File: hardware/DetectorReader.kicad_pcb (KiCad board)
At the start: 2 copper layers, 51.8 x 30 mm, 62 parts, among them J1 10118194-0001LF, J2 Combo_Conn, J3 SMA_Conn, J4 SMA_Conn, J5 SMA_Conn, J6 Conn_Signal, J7 Conn_Amp1, J8 Conn_Amp2, J9 Conn_TriggerOut, Q1 BC847C,215, Q2 BC847C,215, SW1 SeqTrig_SW, U1 ATtiny814-SS, U2 FT231XS-R, U3 XC0900P-10S, U4 MIC5317-3.0YD5-TR, U5 MAX41462GUB+, U6 BA4584RF-E2, U7 MAX4003, Y1 ECS-160-12-37B-CTN-TR

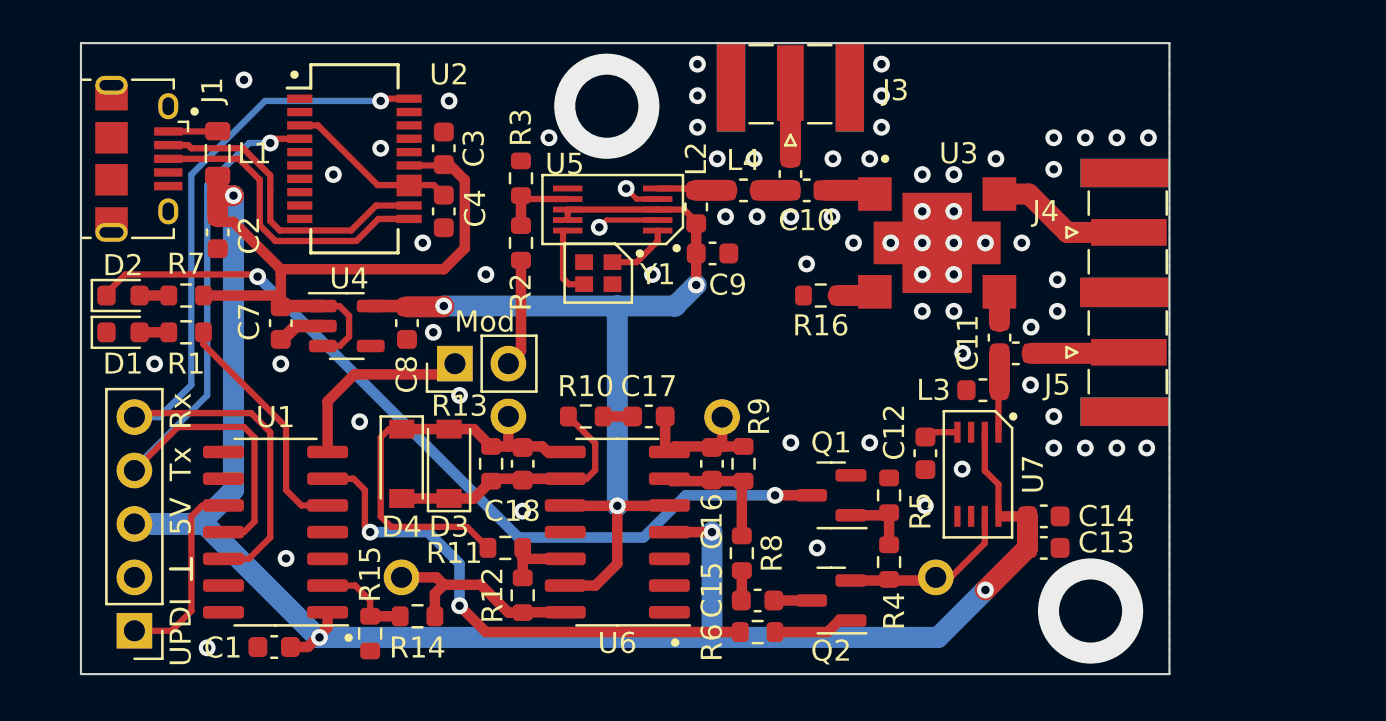
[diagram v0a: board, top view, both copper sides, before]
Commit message: splitted quad opamp into dual opamp and comparator for better digitalization and smaller board
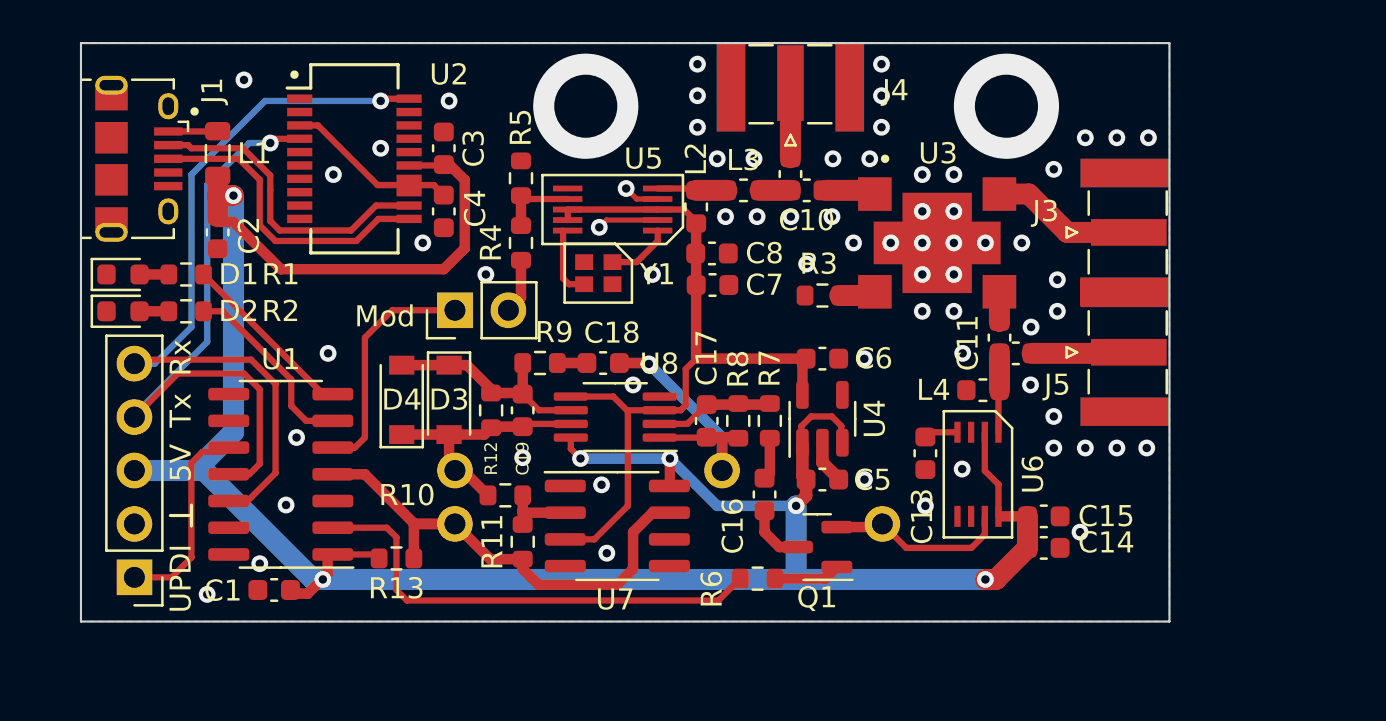
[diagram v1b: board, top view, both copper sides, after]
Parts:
- removed the D2 at (112.0, 84.0)
- removed the Q1 at (145.7, 93.5)
- removed R14: 4.7k, Resistor_SMD:R_0603_1608Metric
- removed R15: 10k, Resistor_SMD:R_0603_1608Metric
- removed the R4 at (148.4, 96.7)
- removed the R5 at (148.4, 93.5)
- removed the R7 at (115.0, 84.0)
- removed the U6 at (135.5, 95.2)
- added C8: 100p, Capacitor_SMD:C_0603_1608Metric, F.Cu at (140.0, 82.0)
- added D1: 150060GS75000, LED_SMD:LED_0603_1608Metric, F.Cu at (112.0, 83.0)
- added R1: 1k, Resistor_SMD:R_0603_1608Metric, F.Cu at (115.0, 83.0)
- added R13: 1k, Resistor_SMD:R_0603_1608Metric, F.Cu at (125.0, 96.5)
- added U7: BA4580RFVM-TR, Package_SO:MSOP-8_3x3mm_P0.65mm, F.Cu at (135.4, 89.8)
- added U8: LM311, Package_SO:SOIC-8_3.9x4.9mm_P1.27mm, F.Cu at (135.5, 95.0)
- moved C5 26.8 mm to (145.2, 92.8), turned to 180 degrees
- moved U4 23.0 mm to (145.2, 89.9), turned to 90 degrees
- moved C6 19.8 mm to (145.2, 87.0), turned to 180 degrees
- moved R7 6.43 mm to (142.8, 90.0)
- moved C16 5.05 mm to (142.5, 93.5), turned to -90 degrees
- moved J8 3.61 mm to (127.8, 92.3)
- moved J9 3.59 mm to (127.8, 94.9)
- moved J6 3.59 mm to (148.1, 94.9)
- moved C18 3.34 mm to (134.8, 87.2)
- moved R9 3.34 mm to (131.8, 87.2)
- moved D3 3.04 mm to (127.5, 89.0), turned to -90 degrees
- moved D4 3.04 mm to (125.2, 89.0), turned to 90 degrees
- moved U1 2.76 mm to (119.5, 92.5)
- moved C1 2.71 mm to (119.2, 98.0)
- moved Q1 2.63 mm to (145.0, 96.0)
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- renumbered C6 to C12, C12 to C13, C13 to C14, C14 to C15, C15 to C16, C16 to C17, C17 to C18, C18 to C19, C7 to C5, C8 to C6, C9 to C7, C5 to C9, D1 to D2, J4 to J3, J3 to J4, L4 to L3, L3 to L4, Q2 to Q1, R11 to R10, R12 to R11, R13 to R12, R1 to R2, R16 to R3, R2 to R4, R3 to R5, R8 to R7, R9 to R8, R10 to R9, U7 to U6
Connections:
- R2 pad 2: /TagDetected -> /TagEPCDetected
- U1 pad 2: /TagPulsesLow -> /SeqProg
- U1 pad 4: unconnected-(U1-Pad4) -> /TagPulses
- U1 pad 5: /TagDetected -> /ReaderPulses
- U1 pad 6: /SeqProg -> /TagEPCDetected
- U1 pad 7: /ReaderPulses -> /TagPreambleDetected
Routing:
- net Net-(D2-Pad1): track 40.0 -> 0.00 mm, vias 2 -> 0
- net /TagPulses: track 10.2 -> 24.5 mm
- net /TagDetected: track 11.4 -> 0.00 mm
- net +3V0: track 46.2 -> 37.1 mm, vias 3 -> 0
- net /TagEPCDetected: track 0.00 -> 9.04 mm
- net /TagPreambleDetected: track 0.00 -> 8.51 mm
- net /RF_Rx/Amp2: track 20.3 -> 12.1 mm
- net /RF_Rx/Amp1: track 6.84 -> 13.3 mm, vias 0 -> 1
- net /TagPulsesLow: track 4.49 -> 0.00 mm
- net +5V: track 115.6 -> 119.8 mm, vias 4 -> 6
- net Net-(Q1-Pad1) (its old number): track 3.39 -> 0.00 mm
- net /uartRx: track 39.8 -> 36.8 mm
- net /RF_Tx/Mod: track 5.16 -> 2.62 mm
- net /uartTx: track 32.8 -> 30.3 mm
- net Net-(C19-Pad2): track 12.8 -> 10.5 mm
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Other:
- board size 51.8 x 30 mm -> 51.8 x 27.5 mm

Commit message: Updated schematic, PCB and fabrication files
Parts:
- removed the C19 at (131.0, 89.5)
- removed D3, D4: 1N4148W_R1_00001, Diode_SMD:D_SOD-123
- removed the R12 at (129.5, 89.5)
- removed the U7 at (135.4, 89.8)
- added C22: 1u, Capacitor_SMD:C_0603_1608Metric, F.Cu at (141.8, 90.2)
- added C24: 100n, Capacitor_SMD:C_0603_1608Metric, F.Cu at (134.0, 93.8)
- added C3: 22u, Capacitor_SMD:C_0603_1608Metric, F.Cu at (121.2, 83.8)
- added C6: 22u, Capacitor_SMD:C_0603_1608Metric, F.Cu at (128.8, 90.8)
- added C7: 22u, Capacitor_SMD:C_0603_1608Metric, F.Cu at (143.0, 92.5)
- added C9: 100p, Capacitor_SMD:C_0603_1608Metric, F.Cu at (132.2, 73.5)
- added L2: MI0805K400R-10, Inductor_SMD:L_0805_2012Metric, F.Cu at (130.5, 93.8)
- added L3: MI0805K400R-10, Inductor_SMD:L_0805_2012Metric, F.Cu at (140.8, 95.5)
- added L4: MI0805K400R-10, Inductor_SMD:L_0805_2012Metric, F.Cu at (129.0, 76.0)
- added Q2: BC847C,215, Package_TO_SOT_SMD:SOT-23, F.Cu at (145.2, 88.2)
- C2: value 10u -> 22u
- C20: renamed from C16; value 100n -> 10n
- C21: renamed from C17; value 100p -> 1n
- C23: renamed from C18; value 3.3n -> 100p
- D1: value 150060GS75000 -> 150060RS75000
- J7: renamed from J8; value Conn_Amp2 -> Conn_CmdInv
- J8: renamed from J7; value Conn_Amp1 -> Conn_Amp
- R10: value 10k -> 6.2k
- R11: value 100k -> 220k
- R7, R9: value 1k -> 220k
- R8: value 27k -> 1k
- moved C8 22.5 mm to (130.5, 75.8), turned to 90 degrees
- moved U4 18.4 mm to (133.0, 76.1), turned to -90 degrees
- moved D1 16.2 mm to (127.8, 87.0), turned to 180 degrees
- moved D2 16.2 mm to (127.8, 88.5), turned to 180 degrees
- moved C10 14.2 mm to (135.3, 76.8), turned to -90 degrees
- moved R1 10.3 mm to (124.8, 86.4), turned to 180 degrees
- moved R2 10.2 mm to (124.8, 87.9), turned to 180 degrees
- moved R9 7.68 mm to (138.5, 91.0), turned to -90 degrees
- moved C11 7.48 mm to (136.7, 76.8), turned to 90 degrees
- moved R10 6.83 mm to (137.0, 93.8), turned to 0 degrees
- moved C20 6.50 mm to (148.0, 90.0)
- moved J9 5.68 mm to (125.2, 89.8)
- moved C12 5.54 mm to (138.1, 76.8), turned to -90 degrees
- moved R12 5.39 mm to (127.0, 91.5), turned to -90 degrees
- moved U7 5.02 mm to (133.8, 90.2), turned to 180 degrees
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- renumbered C6 to C10, C7 to C11, C8 to C12, C9 to C13, C10 to C14, C11 to C15, C12 to C16, C13 to C17, C14 to C18, C15 to C19, C3 to C4, C4 to C5, C5 to C8, L2 to L5, L3 to L6, L4 to L7, R13 to R12, U8 to U7
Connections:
- C1 pad 2: +5V -> +5VDigital
- C18 pad 2: +5V -> +5VAnalog
- C19 pad 2: +5V -> +5VAnalog
- C21 pad 1: /RF_Rx/Amp1 -> +5VAnalog
- C21 pad 2: Net-(C17-Pad2) -> /RF_Rx/Amp
- C23 pad 1: Net-(C18-Pad1) -> /RF_Rx/Avr
- C23 pad 2: /RF_Rx/Amp1 -> GND
- C8 pad 2: +5V -> /RF_Tx/5VLDOIn
- J7 pad 1: /RF_Rx/Amp2 -> /SeqProg
- J8 pad 1: /RF_Rx/Amp1 -> /RF_Rx/Amp
- R10 pad 2: /RF_Rx/Amp2 -> /RF_Rx/Amp
- R12 pad 2: +5V -> +5VDigital
- R7 pad 1: Net-(C17-Pad2) -> /RF_Rx/Amp
- R8 pad 1: /RF_Rx/Amp1 -> +5VAnalog
- R8 pad 2: Net-(C17-Pad2) -> /RF_Rx/Amp
- R9 pad 1: Net-(C19-Pad2) -> /RF_Rx/Avr
- R9 pad 2: Net-(C18-Pad1) -> /RF_Rx/Amp
- U1 pad 1: +5V -> +5VDigital
- U4 pad 1: +5V -> /RF_Tx/5VLDOIn
- U4 pad 3: +5V -> /RF_Tx/5VLDOIn
- U6 pad 2: +5V -> +5VAnalog
- U6 pad 8: +5V -> +5VAnalog
- U7 pad 3: +3V0 -> /RF_Rx/Avr
- U7 pad 8: +5V -> +5VDigital
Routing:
- net +5V: track 119.8 -> 68.7 mm, vias 6 -> 4
- net +5VAnalog: track 0.00 -> 30.2 mm
- net +3V0: track 37.1 -> 12.9 mm
- net /RF_Rx/Amp: track 0.00 -> 20.0 mm
- net +5VDigital: track 0.00 -> 18.7 mm
- net /RF_Rx/Amp1: track 13.3 -> 0.00 mm, vias 1 -> 0
- net /RF_Rx/Amp2: track 12.1 -> 0.00 mm
- net Net-(C19-Pad2): track 10.5 -> 0.00 mm
- net /RF_Tx/5VLDOIn: track 0.00 -> 9.97 mm
- net /TagPulses: track 24.5 -> 16.8 mm
- net /TagEPCDetected: track 9.04 -> 2.15 mm
- net /TagPreambleDetected: track 8.51 -> 2.05 mm
- net Net-(C17-Pad2): track 5.64 -> 0.00 mm
- net /RF_Rx/Avr: track 0.00 -> 3.72 mm
- net Net-(R10-Pad1): track 3.44 -> 7.07 mm
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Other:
- board size 51.8 x 27.5 mm -> 51.8 x 25 mm

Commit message: changed R10 to 12k to increase tag pulse detection trigger threshold
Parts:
- R10: value 6.2k -> 12k
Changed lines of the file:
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@@
       (effects (font (size 0.8 0.8) (thickness 0.15)))
     )
-    (fp_text value "6.2k" (at 0 1.43) (layer "F.Fab")
+    (fp_text value "12k" (at 0 1.43) (layer "F.Fab")
       (effects (font (size 1 1) (thickness 0.15)))
     )
@@
     (property "Sheetfile" "DetectorReader.kicad_sch")
     (property "Sheetname" "")
-    (attr through_hole exclude_from_bom)
+    (attr through_hole)
     (fp_text reference "SW1" (at -2.5 1.54) (layer "F.SilkS") hide
       (effects (font (size 1 1) (thickness 0.15)))
@@
     (property "Sheetfile" "DetectorReader.kicad_sch")
     (property "Sheetname" "")
-    (attr through_hole exclude_from_bom)
+    (attr through_hole)
     (fp_text reference "J2" (at -0.2 12.94) (layer "F.SilkS") hide
       (effects (font (size 1 1) (thickness 0.15)))

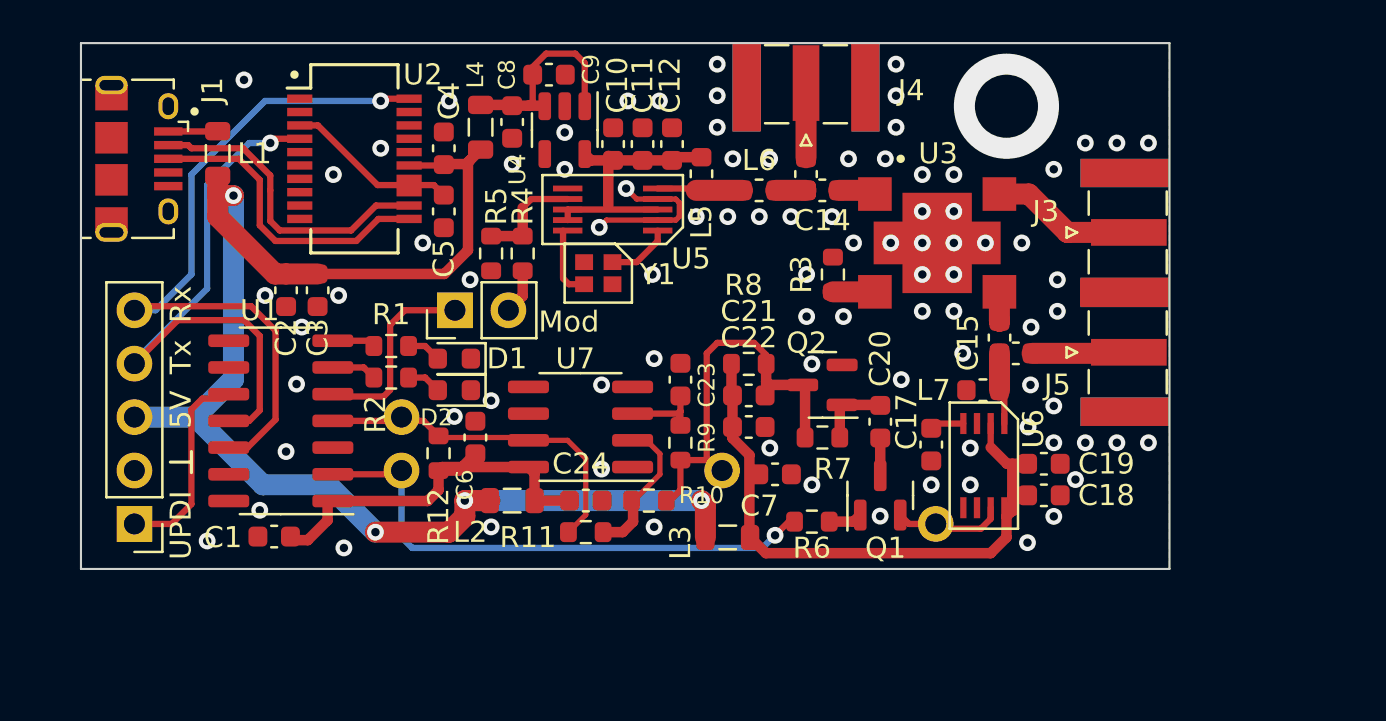
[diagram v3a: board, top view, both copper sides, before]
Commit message: Rev 2. Using USB-C, configurable Tx, op-amp based LF amplifier, tri-color indicator. Using platformIO for firmware, splitted code into separate files.
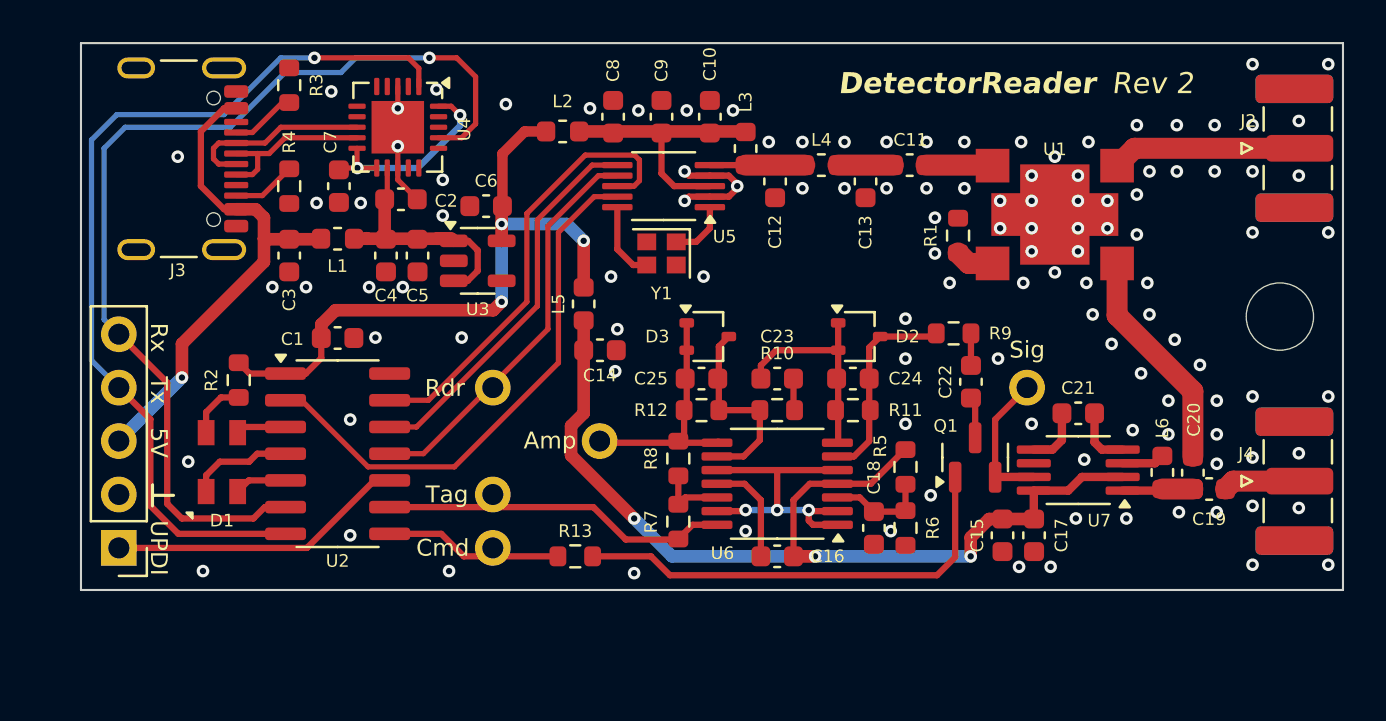
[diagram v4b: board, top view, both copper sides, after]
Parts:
- removed the C10 at (135.3, 76.8)
- removed the C15 at (153.7, 86.0)
- removed the C17 at (150.4, 91.1)
- removed the C7 at (143.0, 92.5)
- removed the C9 at (132.2, 73.5)
- removed the J2 at (112.5, 94.9)
- removed the J4 at (144.5, 74.1)
- removed J6: Conn_Signal, ProjLib:Single_Pin
- removed J7: Conn_CmdInv, ProjLib:Single_Pin
- removed J8: Conn_Amp, ProjLib:Single_Pin
- removed J9: Conn_TriggerOut, ProjLib:Single_Pin
- removed the L3 at (140.8, 95.5)
- removed the L4 at (129.0, 76.0)
- removed L7: 22n, Inductor_SMD:L_0603_1608Metric
- removed Q2: BC847C,215, Package_TO_SOT_SMD:SOT-23
- removed the R2 at (124.8, 87.9)
- removed SW1: SeqTrig_SW, Connector_PinHeader_2.54mm:PinHeader_1x02_P2.54mm_Vertical
- removed the U2 at (123.0, 77.5)
- added C12: 1.2p, Capacitor_SMD:C_0603_1608Metric, F.Cu at (143.0, 78.6)
- added C14: 10u, Capacitor_SMD:C_0603_1608Metric, F.Cu at (134.7, 86.6)
- added C18: 10n, Capacitor_SMD:C_0603_1608Metric, F.Cu at (147.7, 95.0)
- added C19: 1.2p, Capacitor_SMD:C_0603_1608Metric, F.Cu at (163.6, 93.2)
- added C25: 100p, Capacitor_SMD:C_0603_1608Metric, F.Cu at (139.5, 88.0)
- added C3: 100n, Capacitor_SMD:C_0603_1608Metric, F.Cu at (119.9, 82.1)
- added D3: BAV99, Package_TO_SOT_SMD:SOT-323_SC-70, F.Cu at (139.8, 86.0)
- added H1: MountingHole, MountingHole:MountingHole_3.2mm_M3_DIN965, F.Cu at (167.0, 85.0)
- added J3: USB_C_Receptacle_USB2.0_16P, Connector_USB:USB_C_Receptacle_GCT_USB4105-xx-A_16P_TopMnt_Horizontal, F.Cu at (113.7, 77.5)
- added L5: MMZ1608Y301, Inductor_SMD:L_0603_1608Metric, F.Cu at (133.9, 84.4)
- added L6: 29n, Inductor_SMD:L_0603_1608Metric, F.Cu at (161.4, 92.4)
- added R13: 10k, Resistor_SMD:R_0603_1608Metric, F.Cu at (133.5, 96.4)
- added R3: 5.1k, Resistor_SMD:R_0603_1608Metric, F.Cu at (119.9, 74.0)
- added TP1: Rdr, ProjLib:Single_Pin, F.Cu at (129.6, 88.4)
- added TP2: Cmd, ProjLib:Single_Pin, F.Cu at (129.6, 96.0)
- added TP3: Tag, ProjLib:Single_Pin, F.Cu at (129.6, 93.5)
- added TP4: Sig, ProjLib:Single_Pin, F.Cu at (155.0, 88.4)
- added TP5: Amp, ProjLib:Single_Pin, F.Cu at (134.7, 90.9)
- added U3: TLV70330DBVR, Package_TO_SOT_SMD:SOT-23-5, F.Cu at (128.9, 82.3)
- C11: renamed from C14; value 1.5p -> 100p
- C13: value 1.5p -> 2.7p
- C16: value 1.5p -> 100n
- C17: renamed from C19; value 100n -> 10n
- C20: value 10n -> 1.2p
- C22: value 1u -> 10n
- C23: value 100p -> 10n
- C24: value 100n -> 100p
- C4: renamed from C2; value 22u -> 10u
- C5: renamed from C3; value 22u -> 10u
- C6: value 22u -> 1u
- C9: renamed from C11; value 100n -> 10n
- D1: value 150060RS75000 -> IN-P32TATRGB; footprint LED_SMD:LED_0603_1608Metric -> ProjLib:LED_SMD_IN-P32TATRGB
- D2: value 150060GS75000 -> BAV99; footprint LED_SMD:LED_0603_1608Metric -> Package_TO_SOT_SMD:SOT-323_SC-70
- J1: value 10118194-0001LF -> Combo_Conn; footprint Connector_USB:USB_Micro-B_Amphenol_10118194_Horizontal -> Connector_PinHeader_2.54mm:PinHeader_1x05_P2.54mm_Vertical
- J2: renamed from J3; value SMA_Conn -> CON-SMA-EDGE-S; footprint Connector_Coaxial:SMA_Samtec_SMA-J-P-X-ST-EM1_EdgeMount -> Connector_Coaxial:SMA_Samtec_SMA-J-P-H-ST-EM1_EdgeMount
- J4: renamed from J5; value SMA_Conn -> CON-SMA-EDGE-S; footprint Connector_Coaxial:SMA_Samtec_SMA-J-P-X-ST-EM1_EdgeMount -> Connector_Coaxial:SMA_Samtec_SMA-J-P-H-ST-EM1_EdgeMount
- L1, L2: value MI0805K400R-10 -> MMZ1608Y301; footprint Inductor_SMD:L_0805_2012Metric -> Inductor_SMD:L_0603_1608Metric
- L3: renamed from L5; value 29n -> 5.6n
- L4: renamed from L6; value 22n -> 5.6n
- R10: value 12k -> 1k
- R11: value 220k -> 18k
- R12, R8: value 1k -> 18k
- R4: value 1k -> 5.1k
- R5, R6: value 1k -> 10k
- R7: value 220k -> 330k
- R9: value 220k -> 1k
- U4: value MIC5317-3.0YD5-TR -> FT231XQ; footprint Package_TO_SOT_SMD:SOT-23-5 -> Package_DFN_QFN:QFN-20-1EP_4x4mm_P0.5mm_EP2.5x2.5mm
- U5: value MAX41462GUB+ -> MAX41460; footprint ProjLib:uMax-10 -> Package_SO:VSSOP-10_3x3mm_P0.5mm
- U6: value MAX4003 -> TL974IDR; footprint ProjLib:uMax-8 -> Package_SO:TSSOP-14_4.4x5mm_P0.65mm
- U7: value LM311 -> MAX4003; footprint Package_SO:SOIC-8_3.9x4.9mm_P1.27mm -> Package_SO:MSOP-8_3x3mm_P0.65mm
- Y1: footprint ProjLib:Crystal_SMD_2x1.6mm -> Crystal:Crystal_SMD_2016-4Pin_2.0x1.6mm
- moved U7 23.8 mm to (157.4, 92.3)
- moved R5 22.2 mm to (149.2, 92.2)
- moved D2 19.4 mm to (147.0, 86.0), turned to 0 degrees
- moved J1 18.5 mm to (111.8, 96.0), turned to 180 degrees
- moved L2 17.7 mm to (132.9, 76.2)
- moved C21 15.7 mm to (157.4, 89.6), turned to 180 degrees
- moved C20 15.1 mm to (162.9, 92.4), turned to 90 degrees
- moved C16 14.9 mm to (143.1, 96.4), turned to 0 degrees
- moved R9 14.0 mm to (151.5, 85.8), turned to 180 degrees
- moved C24 14.0 mm to (146.7, 88.0), turned to 0 degrees
- moved R11 14.0 mm to (146.7, 89.5), turned to 180 degrees
- moved R12 12.7 mm to (139.5, 89.5), turned to 180 degrees
- moved D1 12.1 mm to (116.7, 91.9), turned to 90 degrees
- moved R4 11.6 mm to (119.9, 78.8)
- moved C6 11.0 mm to (129.3, 79.8), turned to 0 degrees
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- renumbered C12 to C10, C18 to C15, C4 to C2, C5 to C7, R3 to R1, R1 to R2, U3 to U1, U1 to U2
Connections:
- net /RF_Tx/ModOut renamed /RF_Tx/PAOut
- net /RF_Tx/ModOutSelect renamed /RF_Tx/PAMatched
- C1 pad 2: +5VDigital -> +3V0
- C10 pad 2: +3V0 -> /RF_Tx/3VTx
- C13 pad 2: Net-(C13-Pad2) -> GND
- C15 pad 2: +5VAnalog -> /RF_Rx/3VRx
- C16 pad 1: Net-(C16-Pad1) -> GND
- C16 pad 2: Net-(C15-Pad1) -> /RF_Rx/3VRx
- C17 pad 2: +5VAnalog -> /RF_Rx/3VRx
- C20 pad 1: Net-(C20-Pad1) -> Net-(U7-RF_IN)
- C20 pad 2: Net-(C20-Pad2) -> /RF_Rx/DetectorIn
- C21 pad 1: +5VAnalog -> Net-(U7-CLPF)
- C21 pad 2: /RF_Rx/Amp -> GND
- C22 pad 1: GND -> Net-(C22-Pad1)
- C22 pad 2: +5VAnalog -> /RF_Rx/TagSignal
- C23 pad 1: /RF_Rx/Avr -> Net-(C23-Pad1)
- C23 pad 2: GND -> /RF_Rx/Amp1
- C24 pad 1: GND -> /RF_Rx/Amp1
- C24 pad 2: +5VDigital -> Net-(U6B--)
- C6 pad 2: +5VDigital -> +3V0
- C7 pad 2: Net-(C5-Pad2) -> Net-(U4-3V3OUT)
- C8 pad 2: /RF_Tx/5VLDOIn -> /RF_Tx/3VTx
- C9 pad 1: +3V0 -> /RF_Tx/3VTx
- D1 pad 1: GND -> /LEDRed
- D1 pad 2: Net-(D1-Pad2) -> Net-(D1-A)
- D2 pad 1: GND -> /RF_Rx/Amp1
- D2 pad 2: Net-(D2-Pad2) -> /RF_Rx/Amp1
- J1 pad 1: /VBUS -> /UPDI
- J1 pad 2: /USB_N -> GND
- J1 pad 3: /USB_P -> /VBUS
- J1 pad 4: GND -> /uartTx
- J1 pad 5: GND -> /uartRx
- J4 pad 1: Net-(C16-Pad1) -> Net-(J4-In)
- L2 pad 1: +5V -> +3V0
- L2 pad 2: +5VDigital -> /RF_Tx/3VTx
- L3 pad 1: +3V0 -> /RF_Tx/3VTx
- Q1 pad 1: Net-(Q1-Pad1) -> Net-(Q1-B)
- Q1 pad 3: Net-(C20-Pad2) -> /RF_Rx/TagSignal
- R10 pad 1: Net-(R10-Pad1) -> Net-(C23-Pad1)
- R10 pad 2: /RF_Rx/Amp -> Net-(U6C--)
- R11 pad 1: /TagPulses -> Net-(U6B--)
- R11 pad 2: Net-(R10-Pad1) -> /RF_Rx/Amp1
- R12 pad 1: /TagPulses -> Net-(U6C--)
- R12 pad 2: +5VDigital -> /RF_Rx/Amp2
- R2 pad 1: Net-(D1-Pad2) -> +3V0
- R2 pad 2: /TagPreambleDetected -> Net-(D1-A)
- R4 pad 1: /RF_Tx/ModLow -> Net-(J3-CC2)
- R4 pad 2: /RF_Tx/Mod -> GND
- R5 pad 1: /RF_Tx/ModLow -> /RF_Rx/3VRx
- R5 pad 2: GND -> Net-(U6A-+)
- R6 pad 1: /SeqProg -> Net-(U6A-+)
- R6 pad 2: Net-(Q1-Pad1) -> GND
- R7 pad 1: /RF_Rx/Amp -> Net-(U6D-+)
- R7 pad 2: Net-(C20-Pad1) -> /TagPulses
- R8 pad 1: +5VAnalog -> /RF_Rx/Amp2
- R8 pad 2: /RF_Rx/Amp -> Net-(U6D-+)
- R9 pad 1: /RF_Rx/Avr -> Net-(C22-Pad1)
- R9 pad 2: /RF_Rx/Amp -> Net-(U6B--)
- U2 pad 1: +5VDigital -> +3V0
- U2 pad 11: /uartTx -> /SPI.MOSI
- U2 pad 12: /uartRx -> /SPI.MISO
- U2 pad 13: unconnected-(U1-Pad13) -> /SPI.SCK
- U2 pad 2: /SeqProg -> /SPI.~{CS}
- U2 pad 3: unconnected-(U1-Pad3) -> /LEDBlue
- U2 pad 4: /TagPulses -> /LEDRed
- U2 pad 5: /ReaderPulses -> /LEDGreen
- U2 pad 6: /TagEPCDetected -> /uartRx
- U2 pad 7: /TagPreambleDetected -> /uartTx
- U2 pad 8: unconnected-(U1-Pad8) -> /~{ReaderCmd}
- U2 pad 9: unconnected-(U1-Pad9) -> /TagPulses
- U4 pad 1: /RF_Tx/5VLDOIn -> /uartTx
- U4 pad 2: GND -> unconnected-(U4-~{RI}-Pad2)
- U4 pad 3: /RF_Tx/5VLDOIn -> GND
- U4 pad 5: +3V0 -> unconnected-(U4-~{DCD}-Pad5)
- U5 pad 3: +3V0 -> /RF_Tx/3VTx
- U5 pad 6: unconnected-(U5-Pad6) -> /SPI.MISO
- U5 pad 7: /RF_Tx/ModLow -> /SPI.MOSI
- U5 pad 8: +3V0 -> /SPI.SCK
- U5 pad 9: +3V0 -> /SPI.~{CS}
- U6 pad 1: Net-(C15-Pad1) -> /RF_Rx/CM
- U6 pad 2: +5VAnalog -> /RF_Rx/CM
- U6 pad 3: GND -> Net-(U6A-+)
- U6 pad 4: Net-(C17-Pad1) -> /RF_Rx/3VRx
- U6 pad 5: GND -> /RF_Rx/CM
- U6 pad 6: unconnected-(U6-Pad6) -> Net-(U6B--)
- U6 pad 7: /RF_Rx/Signal -> /RF_Rx/Amp1
- U6 pad 8: +5VAnalog -> /RF_Rx/Amp2
- U7 pad 1: GND -> Net-(U7-RF_IN)
- U7 pad 2: Net-(R10-Pad1) -> /RF_Rx/3VRx
- U7 pad 3: /RF_Rx/Avr -> GND
- U7 pad 4: GND -> Net-(U7-CLPF)
- U7 pad 5: unconnected-(U7-Pad5) -> GND
- U7 pad 7: /TagPulses -> /RF_Rx/Signal
- U7 pad 8: +5VDigital -> /RF_Rx/3VRx
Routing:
- net +5V: track 68.7 -> 12.4 mm, vias 4 -> 0
- net /RF_Rx/3VRx: track 0.00 -> 47.8 mm, vias 0 -> 3
- net +5VAnalog: track 30.2 -> 0.00 mm
- net /SeqProg: track 26.1 -> 0.00 mm, vias 1 -> 0
- net /SPI.~{CS}: track 0.00 -> 26.0 mm
- net /VBUS: track 2.36 -> 24.6 mm, vias 0 -> 1
- net Net-(Q1-B): track 0.00 -> 21.8 mm
- net /SPI.SCK: track 0.00 -> 21.4 mm
- net /RF_Rx/Amp: track 20.0 -> 0.00 mm
- net /SPI.MOSI: track 0.00 -> 19.2 mm
- net +3V0: track 12.9 -> 31.9 mm, vias 0 -> 3
- net +5VDigital: track 18.7 -> 0.00 mm
- net /SPI.MISO: track 0.00 -> 18.4 mm
- net /uartTx: track 27.6 -> 43.8 mm
- net /RF_Rx/CM: track 0.00 -> 15.4 mm, vias 0 -> 3
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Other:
- board size 51.8 x 25 mm -> 60 x 26 mm
- board text added: "DetectorReader"
- board text added: "Rev 2"
- board text removed: "Mod"
